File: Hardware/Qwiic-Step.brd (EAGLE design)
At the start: 50.8 x 50.8 mm, 106 parts, among them J1 PTH, J2 Qwiic Right Angle, J3 5.5x2.1mm Barrel, J4 Qwiic Right Angle, J5 ISP, U1 A4988ALT1, U2 ATMEGA328P_TQFP, Y1 16MHz

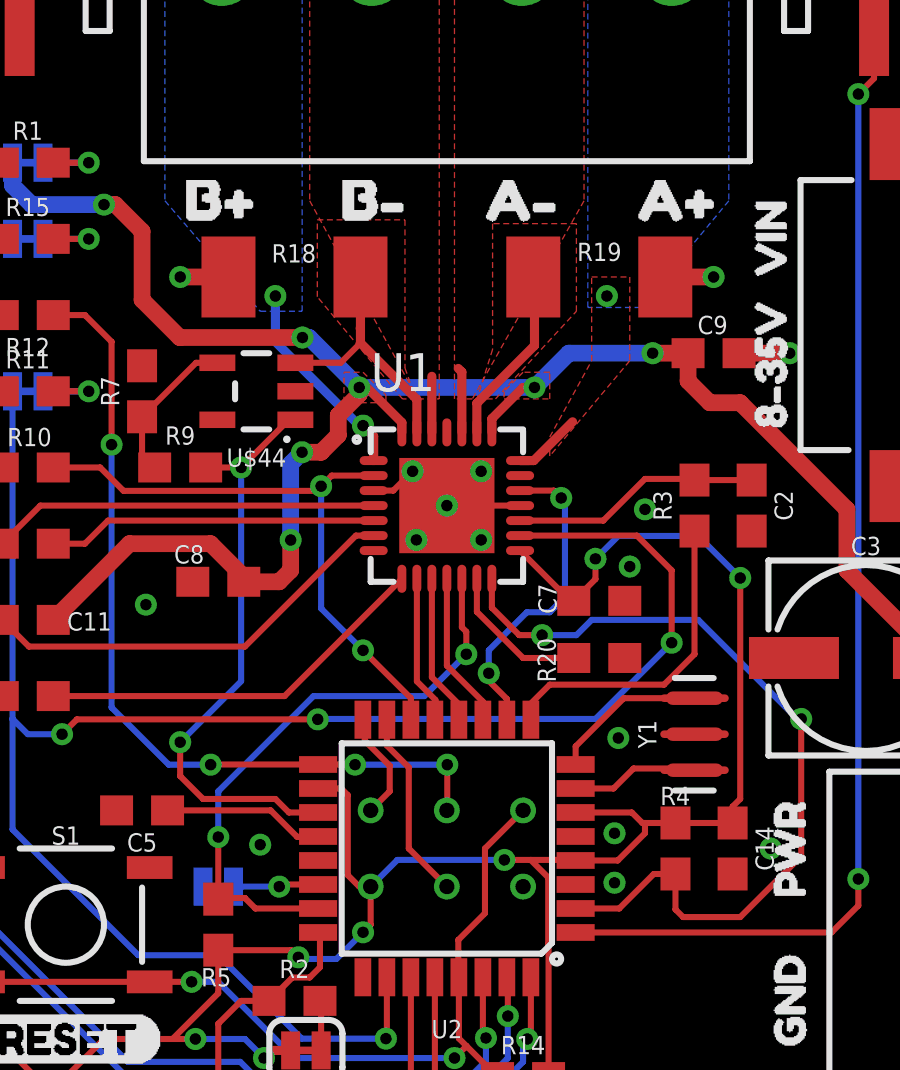
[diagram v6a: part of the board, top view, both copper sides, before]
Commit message: Superficial silk changes. Cleaned up wire stubs
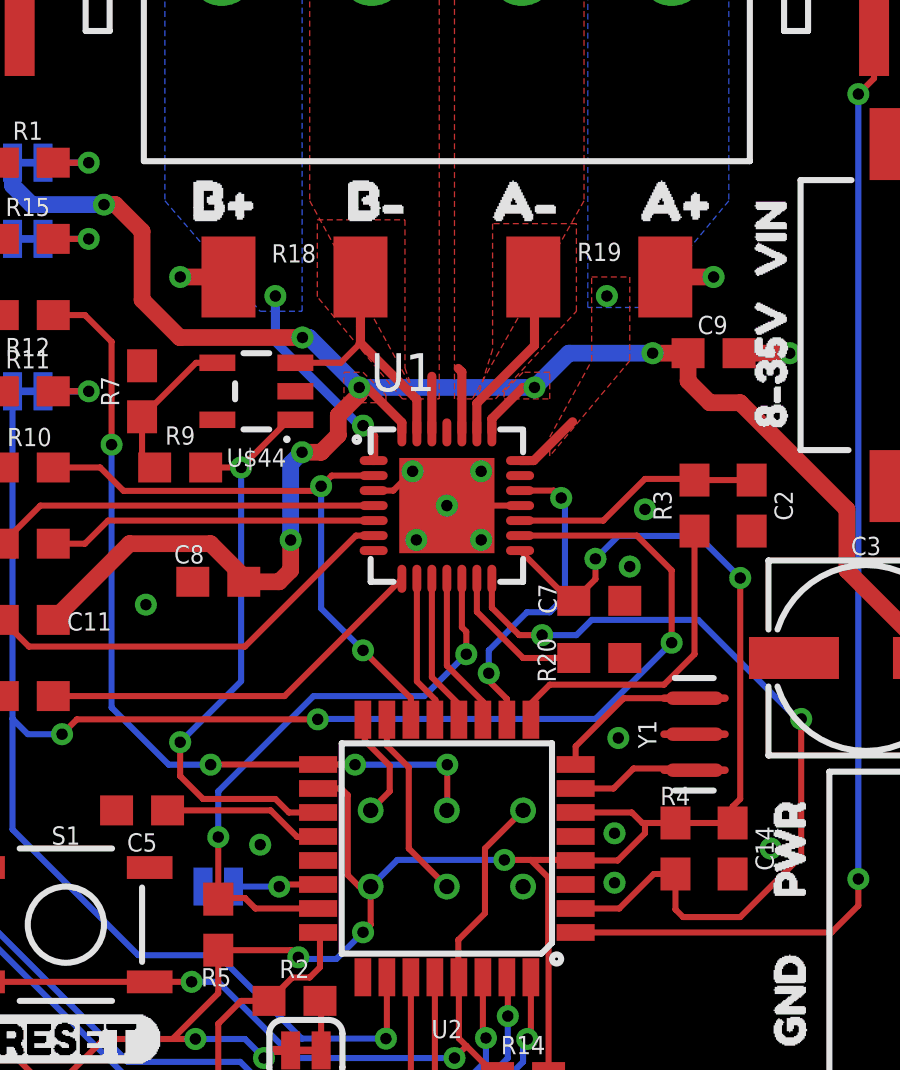
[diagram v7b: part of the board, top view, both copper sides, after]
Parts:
- removed U$15: (no value), buzzard_labels (28):A#3
- removed U$16: (no value), buzzard_labels (28):A#4
- removed U$17, U$48: (no value), buzzard_labels (28):B#5
- removed U$18, U$49: (no value), buzzard_labels (28):B#6
- added U$39: (no value), buzzard_labels (30):A#2
- added U$50: (no value), buzzard_labels (30):A#3
- added U$51: (no value), buzzard_labels (30):B#4
- added U$52: (no value), buzzard_labels (30):B#5
- added U$53: (no value), buzzard_labels (30):GND0
- added U$54: (no value), buzzard_labels (30):PWR1
- added U$56: (no value), buzzard_labels (34):QWIIC_STEP0
- U$32: device buzzard_labels (25):QWIIC_STEP0 -> buzzard_labels (31):A#2
- U$36: device buzzard_labels (28):PWR7 -> buzzard_labels (31):A#3
- U$46: device buzzard_labels (28):A#3 -> buzzard_labels (31):B#4
- U$47: device buzzard_labels (28):A#4 -> buzzard_labels (31):B#5
- moved U$36 26.6 mm to (30.7, 36.8), flipped to the top, turned to 0 degrees
- moved U$47 20.0 mm to (15.7, 36.8), flipped to the top, turned to 0 degrees
- moved U$46 12.3 mm to (21.0, 36.8), flipped to the top, turned to 0 degrees
- moved U$32 11.1 mm to (25.8, 36.8), flipped to the top
- moved LOGO1 2.54 mm to (20.2, 34.0)
- moved U$19 2.54 mm to (27.4, 34.0)
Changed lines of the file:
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@@
 <attribute name="REV" value="" x="-11.78265625" y="-15.24" size="1.778" layer="27" display="off"/>
 </element>
-<element name="LOGO1" library="SparkFun-Aesthetics" package="OSHW-LOGO-MINI" value="OSHW-LOGOMINI" x="20.193" y="31.496" smashed="yes" rot="MR0"/>
+<element name="LOGO1" library="SparkFun-Aesthetics" package="OSHW-LOGO-MINI" value="OSHW-LOGOMINI" x="20.193" y="34.036" smashed="yes" rot="MR0"/>
 <element name="J3" library="SparkFun-Connectors" package="POWER_JACK_SMD" value="5.5x2.1mm Barrel" x="46.99" y="33.02" smashed="yes" rot="R180">
 <attribute name="PROD_ID" value="CONN-08106" x="46.99" y="33.02" size="1.778" layer="27" font="vector" ratio="15" rot="R180" display="off"/>
@@
 </element>
 <element name="U$4" library="buzzard_labels (13)" package="STAT5" value="" x="0.254" y="33.02" smashed="yes"/>
-<element name="U$19" library="SparkX" package="SPARKX-MEDIUM" value="" x="27.432" y="31.496" smashed="yes" rot="MR0"/>
+<element name="U$19" library="SparkX" package="SPARKX-MEDIUM" value="" x="27.432" y="34.036" smashed="yes" rot="MR0"/>
 <element name="U$20" library="buzzard_labels" package="BLK2" value="" x="3.175" y="8.89" smashed="yes"/>
 <element name="U$21" library="buzzard_labels" package="BLK2" value="" x="7.62" y="8.89" smashed="yes" rot="MR0"/>
@@
 <element name="U$29" library="SparkFun-Aesthetics" package="QWIIC_5.5MM" value="" x="42.926" y="3.175" smashed="yes" rot="R90"/>
 <element name="U$30" library="buzzard_labels (16)" package="INT4" value="" x="20.32" y="1.651" smashed="yes" rot="MR90"/>
-<element name="U$32" library="buzzard_labels (25)" package="QWIIC_STEP0" value="" x="36.83" y="35.56" smashed="yes" rot="MR0"/>
 <element name="U$26" library="buzzard_labels (19)" package="3V35" value="" x="27.94" y="1.524" smashed="yes" rot="MR90"/>
 <element name="U$31" library="buzzard_labels (19)" package="GND6" value="" x="30.48" y="1.524" smashed="yes" rot="MR90"/>
@@
 </element>
 <element name="U$45" library="buzzard_labels (28)" package="3V31" value="" x="8.89" y="35.56" smashed="yes" rot="MR0"/>
-<element name="U$46" library="buzzard_labels (28)" package="A#3" value="" x="27.94" y="46.99" smashed="yes" rot="MR90"/>
-<element name="U$47" library="buzzard_labels (28)" package="A#4" value="" x="33.02" y="46.99" smashed="yes" rot="MR90"/>
-<element name="U$48" library="buzzard_labels (28)" package="B#5" value="" x="17.78" y="46.99" smashed="yes" rot="MR90"/>
-<element name="U$49" library="buzzard_labels (28)" package="B#6" value="" x="22.86" y="46.99" smashed="yes" rot="MR90"/>
-<element name="U$36" library="buzzard_labels (28)" package="PWR7" value="" x="41.91" y="12.7" smashed="yes" rot="MR90"/>
 <element name="U$37" library="buzzard_labels (28)" package="STEP2" value="" x="8.89" y="30.48" smashed="yes" rot="MR0"/>
 <element name="U$38" library="buzzard_labels (28)" package="VIN0" value="" x="8.89" y="38.1" smashed="yes" rot="MR0"/>
-<element name="U$15" library="buzzard_labels (28)" package="A#3" value="" x="30.861" y="36.703" smashed="yes"/>
-<element name="U$16" library="buzzard_labels (28)" package="A#4" value="" x="25.781" y="36.703" smashed="yes"/>
-<element name="U$17" library="buzzard_labels (28)" package="B#5" value="" x="15.748" y="36.703" smashed="yes"/>
-<element name="U$18" library="buzzard_labels (28)" package="B#6" value="" x="20.955" y="36.703" smashed="yes"/>
+<element name="U$39" library="buzzard_labels (30)" package="A#2" value="" x="33.02" y="46.99" smashed="yes" rot="MR90"/>
+<element name="U$50" library="buzzard_labels (30)" package="A#3" value="" x="27.94" y="46.99" smashed="yes" rot="MR90"/>
+<element name="U$51" library="buzzard_labels (30)" package="B#4" value="" x="22.86" y="46.99" smashed="yes" rot="MR90"/>
+<element name="U$52" library="buzzard_labels (30)" package="B#5" value="" x="17.78" y="46.99" smashed="yes" rot="MR90"/>
+<element name="U$53" library="buzzard_labels (30)" package="GND0" value="" x="41.91" y="6.858" smashed="yes" rot="MR90"/>
+<element name="U$54" library="buzzard_labels (30)" package="PWR1" value="" x="41.91" y="12.065" smashed="yes" rot="MR90"/>
+<element name="U$56" library="buzzard_labels (34)" package="QWIIC_STEP0" value="" x="43.18" y="38.1" smashed="yes" rot="MR0"/>
+<element name="U$32" library="buzzard_labels (31)" package="A#2" value="" x="25.781" y="36.83" smashed="yes"/>
+<element name="U$36" library="buzzard_labels (31)" package="A#3" value="" x="30.734" y="36.83" smashed="yes"/>
+<element name="U$46" library="buzzard_labels (31)" package="B#4" value="" x="20.955" y="36.83" smashed="yes"/>
+<element name="U$47" library="buzzard_labels (31)" package="B#5" value="" x="15.748" y="36.83" smashed="yes"/>
 </elements>
 <signals>
@@
 <contactref element="J8" pad="2"/>
 <contactref element="J9" pad="2"/>
-<wire x1="29.6926" y1="14.04" x2="29.6226" y2="13.97" width="0.254" layer="1"/>
 <wire x1="27.8399" y1="26.67" x2="26.67" y2="26.67" width="0.2032" layer="1"/>
 <wire x1="35.14" y1="31.75" x2="36.83" y2="31.75" width="0.5588" layer="1"/>
@@
 <wire x1="22.52" y1="32.09" x2="22.52" y2="32.639" width="0.3048" layer="1"/>
 <wire x1="22.52" y1="32.639" x2="22.52" y2="34.29" width="0.3048" layer="1"/>
-<wire x1="22.4565" y1="32.5755" x2="22.52" y2="32.639" width="0.2032" layer="1"/>
 <wire x1="20.3501" y1="31.43" x2="21.86" y2="31.43" width="0.2032" layer="1"/>
 <wire x1="21.86" y1="31.43" x2="22.52" y2="32.09" width="0.2032" layer="1"/>
@@
 <contactref element="C11" pad="2"/>
 <contactref element="JP1" pad="2"/>
-<wire x1="33.313" y1="31.877" x2="33.44" y2="31.75" width="0.5588" layer="1"/>
 <contactref element="C1" pad="1"/>
 <contactref element="D1" pad="C"/>
@@
 <contactref element="U$44" pad="1"/>
 <contactref element="U2" pad="19"/>
-<wire x1="21.1074" y1="16.44" x2="21.0946" y2="16.4272" width="0.2032" layer="1"/>
 <wire x1="21.1074" y1="16.44" x2="20.136" y2="16.44" width="0.2032" layer="1"/>
 <wire x1="19.685" y1="16.891" x2="20.136" y2="16.44" width="0.2032" layer="1"/>
 <contactref element="R9" pad="2"/>
-<wire x1="20.3501" y1="29.53" x2="20.3501" y2="29.4941" width="0.2032" layer="1"/>
 <via x="18.542" y="27.94" extent="1-16" drill="0.381"/>
 <via x="16.51" y="18.7833" extent="1-16" drill="0.381"/>

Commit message: Rev X02 finally done?
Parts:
- removed FRAME1: FRAME-LETTER, SparkFun-Aesthetics:CREATIVE_COMMONS
- removed JP2: ADR, SparkFun-Jumpers:SMT-JUMPER_2_NC_TRACE_SILK
- removed U$39: (no value), buzzard_labels (30):A#2
- removed U$50: (no value), buzzard_labels (30):A#3
- removed U$51: (no value), buzzard_labels (30):B#4
- removed U$52: (no value), buzzard_labels (30):B#5
- added ADR: ADR, SparkFun-Jumpers:SMT-JUMPER_2_NO_SILK
- added C12: 0.1uF, SparkFun-Capacitors:0603
- added FD1, FD2, FD3, FD4: FIDUCIAL1X2, SparkFun-Aesthetics:FIDUCIAL-1X2
- added FRAME2: FRAME-LEDGER, SparkFun-Aesthetics:CREATIVE_COMMONS
- added R6, R8: 2.2k, SparkFun-Resistors:0603
- added SCK, VIN: JUMPER-SMT_2_NC_TRACE_SILK, SparkFun-Jumpers:SMT-JUMPER_2_NC_TRACE_SILK
- added U$17: (no value), buzzard_labels (38):3V31
- added U$18: (no value), buzzard_labels (38):DTR4
- added U$48: (no value), buzzard_labels (38):TXO2
- added U$49: SPARKX-LOGO4, SparkX:SPARKX-MEDIUM
- added U$55: (no value), buzzard_labels (42):A#3
- added U$57: (no value), buzzard_labels (42):B#4
- added U$58: (no value), buzzard_labels (42):B#5
- added U44: OPA344, SparkFun-IC-Amplifiers:SOT23-5
- D2: value GREEN -> BLUE
- D3: value BLUE -> GREEN
- JP1: value JUMPER-SMT_2_NC_TRACE_SILK -> (none); device SparkFun-Jumpers:SMT-JUMPER_2_NC_TRACE_SILK -> SparkFun-Jumpers:SMT-JUMPER_3_2-NC_TRACE_SILK
- R11: value 470 -> 1k
- R12: value 4.7k -> 470
- U$13: device buzzard_labels (16):VIN1 -> buzzard_labels (16):8#35V0
- U$19: device SparkX:SPARKX-MEDIUM -> buzzard_labels (39):DEBUG0
- U$21: device buzzard_labels:BLK2 -> buzzard_labels (38):GND0
- U$22: device buzzard_labels:GRN1 -> buzzard_labels (38):GND0
- U$35: device buzzard_labels (26):PROG0 -> buzzard_labels (38):RXI3
- U$40: device buzzard_labels (27):SERIAL0 -> buzzard_labels (16):8#35V0
- U$44: value OPA344 -> (none); device SparkFun-IC-Amplifiers:SOT23-5 -> buzzard_labels (42):GND0
- U$53: device buzzard_labels (30):GND0 -> buzzard_labels (42):PWR1
- U$54: device buzzard_labels (30):PWR1 -> buzzard_labels (42):A#2
- moved U$40 39.6 mm to (44.5, 6.35), turned to 0 degrees
- moved U$44 38.0 mm to (51.2, 10.2), flipped to the bottom, turned to 0 degrees
- moved U$54 35.0 mm to (32.8, 45.8)
- moved JP1 34.3 mm to (33.0, 11.4)
- moved U$19 33.2 mm to (4.70, 9.78), flipped to the top, turned to 90 degrees
- moved U$13 24.8 mm to (47.4, 35.6), turned to 0 degrees
- moved U$11 14.9 mm to (50.9, 12.7), turned to 0 degrees
- moved U$22 12.8 mm to (6.48, 8.89)
- moved U$53 12.6 mm to (51.3, 15.2), turned to 0 degrees
- moved C10 11.5 mm to (22.9, 22.0), turned to 270 degrees
- moved R10 8.26 mm to (19.1, 24.8)
- moved C6 8.03 mm to (19.1, 22.9)
- moved C11 7.85 mm to (19.1, 21.0), turned to 180 degrees
- moved C8 7.73 mm to (19.1, 31.8)
- moved U$35 5.60 mm to (5.71, 16.5), turned to 0 degrees
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- renumbered JP11 to STEP, JP13 to 3V3
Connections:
- new net N$15: JP1.3, R6.2
- new net N$16: JP1.1, R8.2
- new net N$17: R12.2, SCK.1
- net 3.3V: now also C12.1, JP1.2, U44.5
- net AMP_CUR_SENSE: now also U44.1; no longer U$44.1
- net COILA+: now also J6.P$4; no longer J6.4
- net COILA-: now also J6.P$3; no longer J6.3
- net COILB+: now also J6.P$1; no longer J6.1
- net COILB-: now also J6.P$2; no longer J6.2
- net CURRENT_SENSE: now also U44.3; no longer U$44.3
- net GND: now also ADR.2, C12.2, J9.P$2, U44.2; no longer J9.2, JP2.2
- net N$12: now also R12.1; no longer R12.2
- net N$2: now also U44.4; no longer U$44.4
- net N$4: now also VIN.1; no longer JP1.1
- net N$6: now also ADR.1; no longer JP2.1
- net N$7: now also J9.P$1; no longer J9.1
- net SCK: now also SCK.2; no longer R12.1
- net SCL: now also R8.1
- net SDA: now also R6.1
- net VIN: now also VIN.2; no longer JP1.2
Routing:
- net DIR: track 10.7 -> 35.1 mm, vias 2 -> 4
- net 3.3V: track 147.3 -> 169.5 mm, vias 11 -> 12
- net A49885_!RESET!: track 19.8 -> 37.3 mm
- net SDA: track 39.8 -> 56.0 mm
- net N$20: track 13.2 -> 2.34 mm
- net !ENABLE!: track 20.2 -> 31.1 mm
- net N$21: track 14.3 -> 6.40 mm
- net COILA+: track 2.29 -> 8.64 mm
- net N$9: track 11.0 -> 5.23 mm
- net N$8: track 12.9 -> 7.24 mm
- net STEP: track 63.4 -> 67.3 mm
- net N$17: track 0.00 -> 3.61 mm, vias 0 -> 1
- net AMP_CUR_SENSE: track 19.9 -> 23.2 mm
- net N$7: track 21.3 -> 18.4 mm, vias 1 -> 0
- net N$15: track 0.00 -> 2.70 mm, vias 0 -> 1
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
